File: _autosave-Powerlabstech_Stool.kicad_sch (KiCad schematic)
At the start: 54 parts, among them J1 Screw_Terminal_01x02, J2 Conn_01x02_Pin, J3 Conn_01x02_Pin, J4 Conn_01x05_Socket, J5 Screw_Terminal_01x02, K1 SANYOU_SRD_Form_C, Q1 Q_NMOS_GSD, Q2 Q_NMOS_GSD, Q3 Q_NMOS_GSD, Q4 Q_NMOS_GSD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

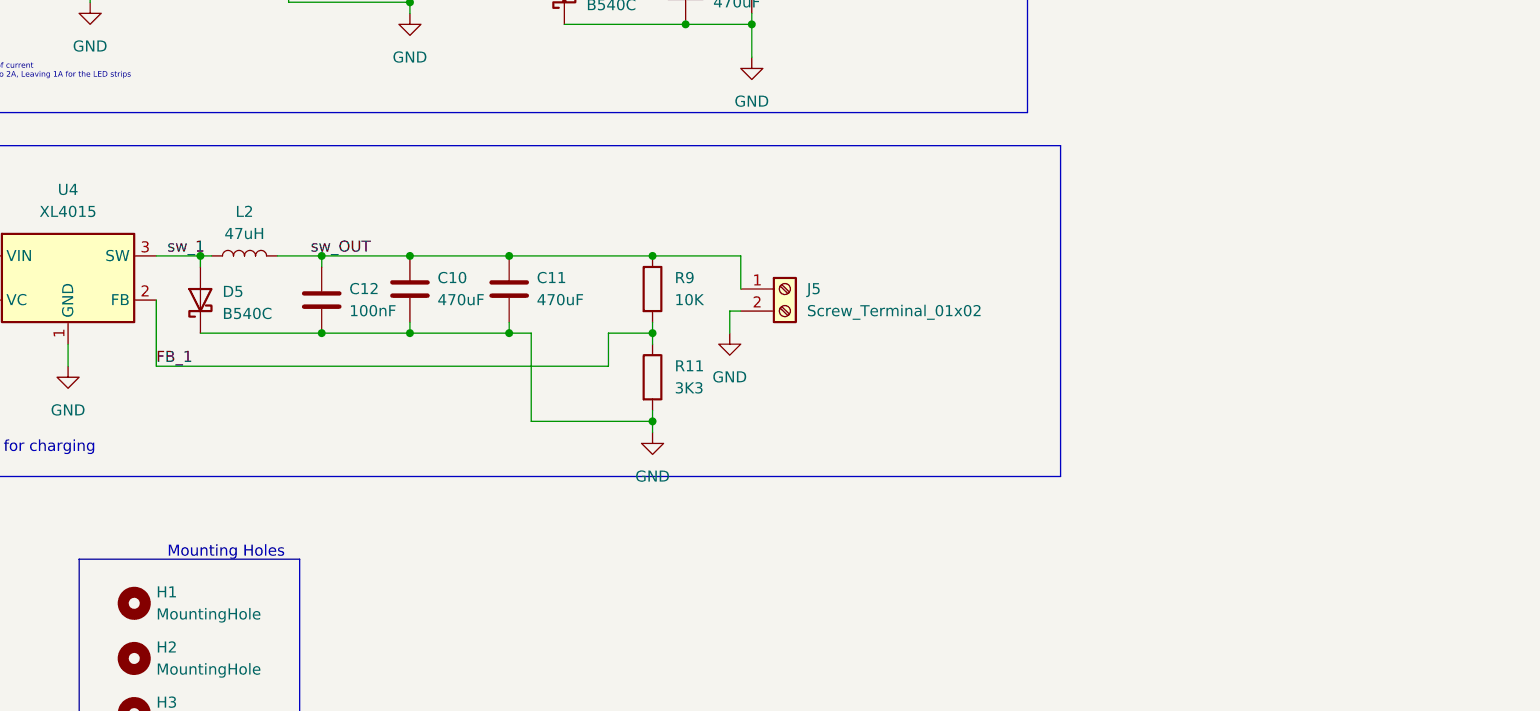
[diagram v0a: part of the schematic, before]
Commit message: Added the USB output and added the output files
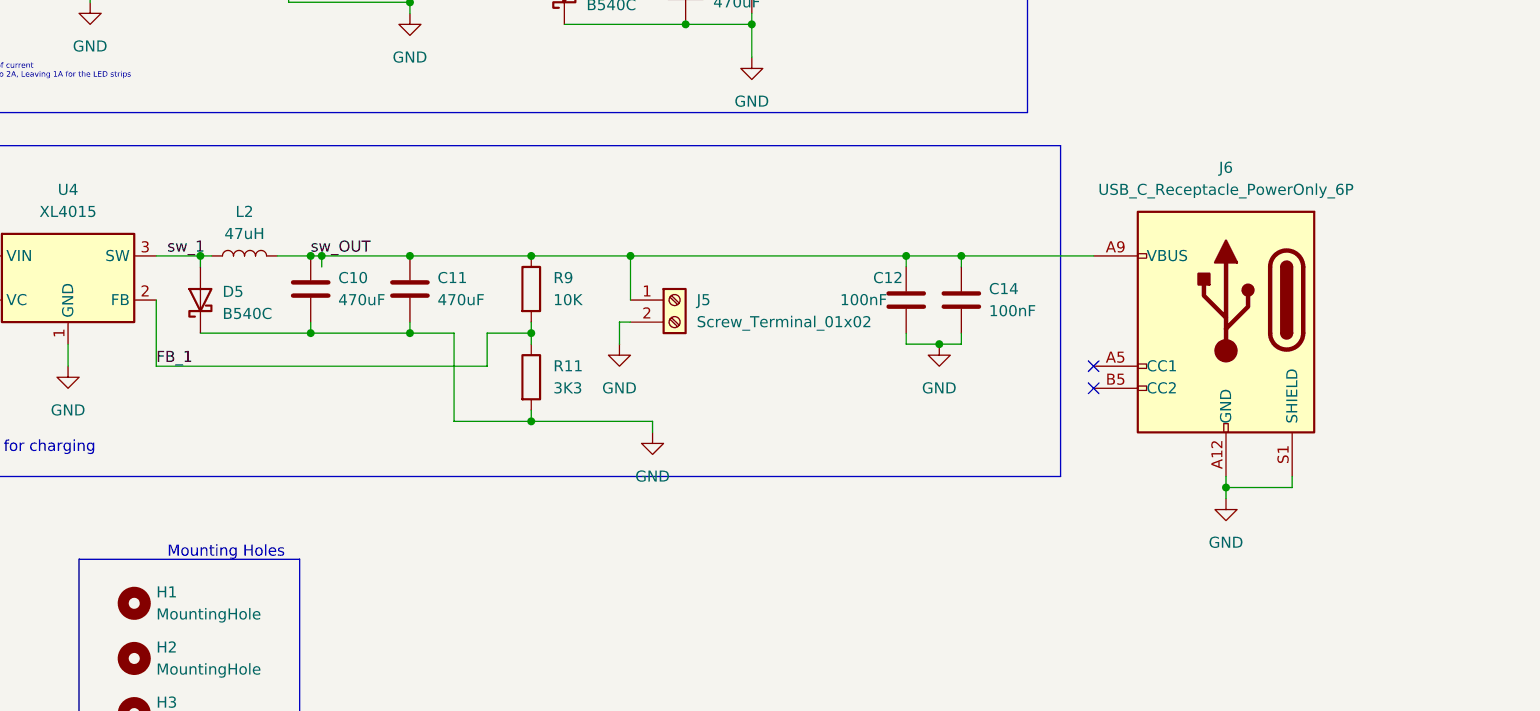
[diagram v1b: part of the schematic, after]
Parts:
- added C14: 100nF, Capacitor_SMD:C_0603_1608Metric, symbol Device:C
- added J6: USB_C_Receptacle_PowerOnly_6P, Connector_USB:USB_C_Receptacle_GCT_USB4125-xx-x_6P_TopMnt_Horizontal, symbol Connector:USB_C_Receptacle_PowerOnly_6P
- D3: footprint TerminalBlock:TerminalBlock_bornier-4_P5.08mm -> TerminalBlock_Phoenix:TerminalBlock_Phoenix_MKDS-3-4-5.08_1x04_P5.08mm_Horizontal
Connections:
- net GND: now also C14.2, J6.A12 (GND), J6.B12 (GND), J6.S1 (SHIELD)
- net sw_OUT: now also C14.1, J6.A9 (VBUS), J6.B9 (VBUS)
- no-connect marks 23 -> 25
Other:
- moved on the sheet: C10, C11, C12, J5, R11, R9
